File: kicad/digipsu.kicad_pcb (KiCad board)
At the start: 2 copper layers, 57 parts, among them J1 Screw_Terminal_01x03, J2 Screw_Terminal_01x03, Q1 BC337, Q2 BC327, Q3 2N6058, Q4 2N6058, Q5 IRLZ34N, U1 INA169, U2 MCP6002-xP, U3 Pico, U4 MCP6002-xP

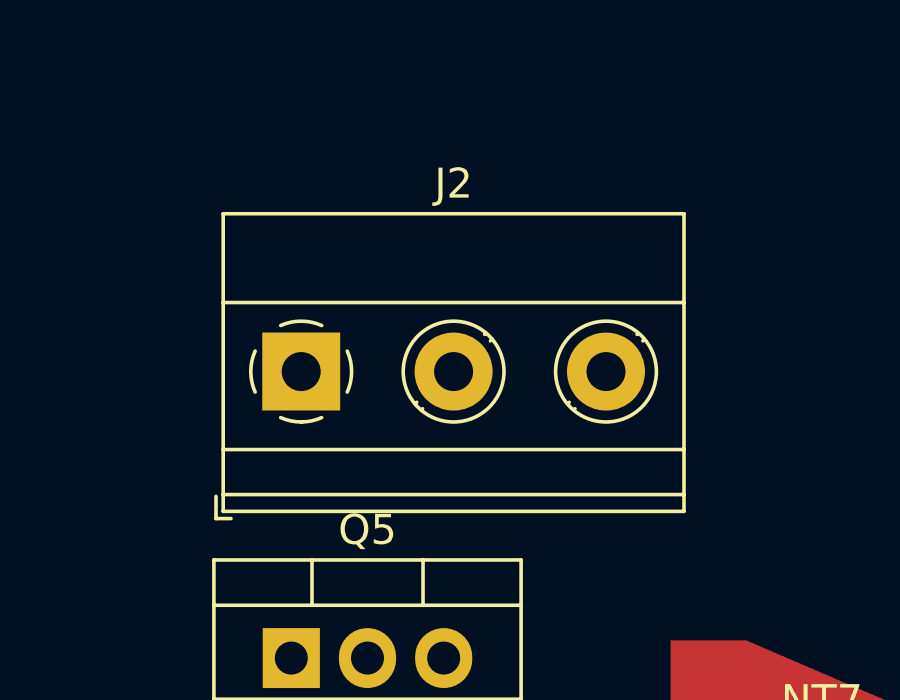
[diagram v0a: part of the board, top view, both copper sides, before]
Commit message: Small change for KiBot testing
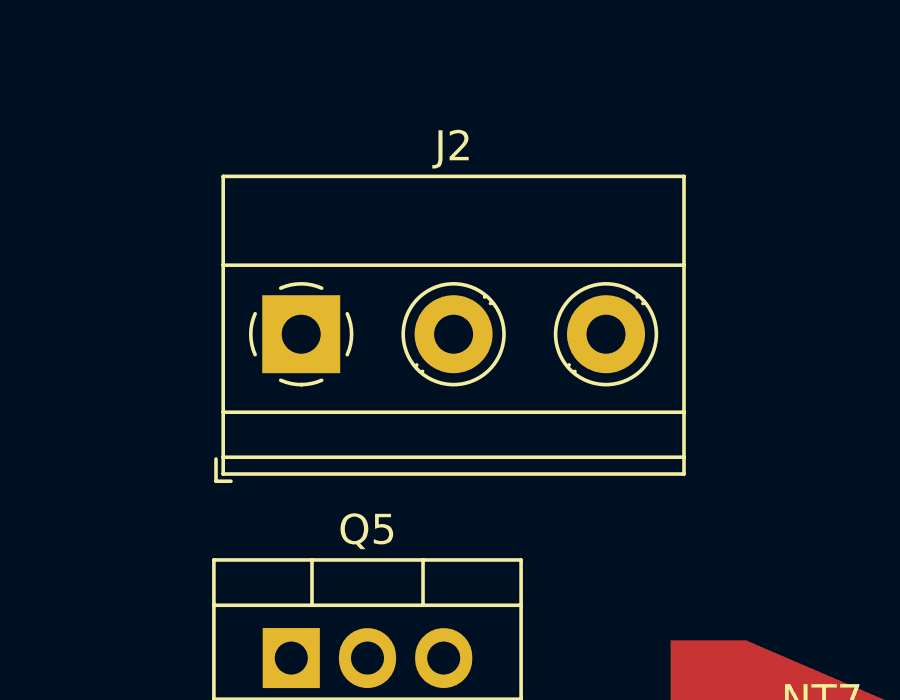
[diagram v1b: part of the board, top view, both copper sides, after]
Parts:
- moved J2 1.24 mm to (34.7, 27.9)
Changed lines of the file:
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@@
   )
   (footprint "TerminalBlock_Phoenix:TerminalBlock_Phoenix_MKDS-1,5-3-5.08_1x03_P5.08mm_Horizontal" (layer "F.Cu")
-    (at 34.715 29.185)
+    (at 34.715 27.94)
     (descr "Terminal Block Phoenix MKDS-1,5-3-5.08, 3 pins, pitch 5.08mm, size 15.2x9.8mm^2, drill diamater 1.3mm, pad diameter 2.6mm, see http://www.farnell.com/datasheets/100425.pdf, script-generated using https://github.com/pointhi/kicad-footprint-generator/scripts/TerminalBlock_Phoenix")
     (tags "THT Terminal Block Phoenix MKDS-1,5-3-5.08 pitch 5.08mm size 15.2x9.8mm^2 drill 1.3mm pad 2.6mm")

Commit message: Complete controller board
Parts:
- removed NT7: NetTie_2, Personal:NetTie_5mm_0.635mm
- added C1: C, Capacitor_THT:C_Disc_D3.8mm_W2.6mm_P2.50mm, F.Cu at (137.2, 83.8)
- added C10: C, Capacitor_THT:C_Disc_D3.8mm_W2.6mm_P2.50mm, F.Cu at (33.7, 144.1)
- added C11: C, Capacitor_THT:C_Disc_D3.8mm_W2.6mm_P2.50mm, F.Cu at (83.8, 189.2)
- added C12: 10µ, Capacitor_THT:C_Disc_D3.8mm_W2.6mm_P2.50mm, F.Cu at (67.9, 195.5)
- added C13: 100n, Capacitor_THT:C_Disc_D3.8mm_W2.6mm_P2.50mm, F.Cu at (64.8, 195.5)
- added C14: 100n, Capacitor_THT:C_Disc_D3.8mm_W2.6mm_P2.50mm, F.Cu at (38.1, 179.1)
- added C15: 100n, Capacitor_THT:C_Disc_D3.8mm_W2.6mm_P2.50mm, F.Cu at (21.6, 151.8)
- added C16: 10n, Capacitor_THT:C_Disc_D3.8mm_W2.6mm_P2.50mm, F.Cu at (102.2, 150.5)
- added C2: C, Capacitor_THT:C_Disc_D3.8mm_W2.6mm_P2.50mm, F.Cu at (137.2, 88.0)
- added C3: C, Capacitor_THT:C_Disc_D3.8mm_W2.6mm_P2.50mm, F.Cu at (137.2, 92.1)
- added C4: C, Capacitor_THT:C_Disc_D3.8mm_W2.6mm_P2.50mm, F.Cu at (96.5, 189.2)
- added C5: C, Capacitor_THT:C_Disc_D3.8mm_W2.6mm_P2.50mm, F.Cu at (91.4, 189.2)
- added C6: 10µ, Capacitor_THT:C_Disc_D3.8mm_W2.6mm_P2.50mm, F.Cu at (55.2, 195.5)
- added C7: 100n, Capacitor_THT:C_Disc_D3.8mm_W2.6mm_P2.50mm, F.Cu at (58.4, 195.5)
- added C8: 10µ, Capacitor_THT:C_Disc_D3.8mm_W2.6mm_P2.50mm, F.Cu at (73.0, 188.0)
- added C9: 100n, Capacitor_THT:C_Disc_D3.8mm_W2.6mm_P2.50mm, F.Cu at (69.8, 188.0)
- added H1: MountingHole, MountingHole:MountingHole_5mm, F.Cu at (24.1, 189.2)
- added H2: MountingHole, MountingHole:MountingHole_5mm, F.Cu at (110.5, 158.8)
- added H3: MountingHole, MountingHole:MountingHole_5mm, F.Cu at (50.8, 148.6)
- added J3: 8P8C, Connector_RJ:RJ45_Amphenol_54602-x08_Horizontal, F.Cu at (102.9, 191.8)
- added J4: 8P8C, Connector_RJ:RJ45_Amphenol_54602-x08_Horizontal, F.Cu at (27.9, 137.2)
- added J5: 8P8C, Connector_RJ:RJ45_Amphenol_54602-x08_Horizontal, F.Cu at (260.0, 96.3)
- added PS1: 1S4AE_1205S1.5UP, Converter_DCDC:Converter_DCDC_Murata_MEE1SxxxxSC_THT, F.Cu at (43.2, 147.3)
- added R39: 10k, Resistor_THT:R_Axial_DIN0207_L6.3mm_D2.5mm_P7.62mm_Horizontal, F.Cu at (78.1, 67.1)
- added R40: 1k, Resistor_THT:R_Axial_DIN0207_L6.3mm_D2.5mm_P7.62mm_Horizontal, F.Cu at (78.1, 71.1)
- added R41: 200, Potentiometer_THT:Potentiometer_Bourns_3296W_Vertical, F.Cu at (110.8, 89.3)
- added R42: 10, Resistor_THT:R_Axial_DIN0207_L6.3mm_D2.5mm_P7.62mm_Horizontal, F.Cu at (44.5, 188.0)
- added R43: 10, Resistor_THT:R_Axial_DIN0207_L6.3mm_D2.5mm_P7.62mm_Horizontal, F.Cu at (34.3, 188.0)
- added R44: 10, Resistor_THT:R_Axial_DIN0207_L6.3mm_D2.5mm_P7.62mm_Horizontal, F.Cu at (48.3, 184.2)
- added R45: 10, Resistor_THT:R_Axial_DIN0207_L6.3mm_D2.5mm_P7.62mm_Horizontal, F.Cu at (76.2, 195.6)
- added R46: 10, Resistor_THT:R_Axial_DIN0207_L6.3mm_D2.5mm_P7.62mm_Horizontal, F.Cu at (80.0, 195.6)
- added R47: 100, Resistor_THT:R_Axial_DIN0207_L6.3mm_D2.5mm_P7.62mm_Horizontal, F.Cu at (113.7, 176.5)
- added R48: 100, Resistor_THT:R_Axial_DIN0207_L6.3mm_D2.5mm_P7.62mm_Horizontal, F.Cu at (110.5, 176.5)
- added R49: 10k, Resistor_THT:R_Axial_DIN0207_L6.3mm_D2.5mm_P7.62mm_Horizontal, F.Cu at (29.2, 90.2)
- added R50: 10k, Resistor_THT:R_Axial_DIN0207_L6.3mm_D2.5mm_P7.62mm_Horizontal, F.Cu at (26.7, 93.3)
- added R51: 100, Resistor_THT:R_Axial_DIN0207_L6.3mm_D2.5mm_P7.62mm_Horizontal, F.Cu at (29.8, 167.6)
- added R52: 1k, Resistor_THT:R_Axial_DIN0207_L6.3mm_D2.5mm_P7.62mm_Horizontal, F.Cu at (29.8, 162.6)
- added R53: 100, Resistor_THT:R_Axial_DIN0207_L6.3mm_D2.5mm_P7.62mm_Horizontal, F.Cu at (19.1, 179.1)
- added R54: 1k, Resistor_THT:R_Axial_DIN0207_L6.3mm_D2.5mm_P7.62mm_Horizontal, F.Cu at (43.8, 175.3)
- added R55: 100, Resistor_THT:R_Axial_DIN0207_L6.3mm_D2.5mm_P7.62mm_Horizontal, F.Cu at (43.8, 154.9)
- added R56: 100, Resistor_THT:R_Axial_DIN0207_L6.3mm_D2.5mm_P7.62mm_Horizontal, F.Cu at (104.1, 176.5)
- added R57: 100, Resistor_THT:R_Axial_DIN0207_L6.3mm_D2.5mm_P7.62mm_Horizontal, F.Cu at (107.3, 176.5)
- added R58: 100, Resistor_THT:R_Axial_DIN0207_L6.3mm_D2.5mm_P7.62mm_Horizontal, F.Cu at (233.3, 105.3)
- added U10: Pico, MCU_RaspberryPi_and_Boards:RPi_Pico_SMD_TH, F.Cu at (219.7, 118.1)
- added U11: M24C32-RMN, Package_SO:SOIC-8_3.9x4.9mm_P1.27mm, F.Cu at (33.0, 85.7)
- added U12: SN75176BP, Package_DIP:DIP-8_W7.62mm, F.Cu at (26.7, 175.3)
- added U13: 6N137, Package_DIP:DIP-8_W7.62mm, F.Cu at (33.0, 167.6)
- added U14: SN75176BP, Package_DIP:DIP-8_W7.62mm, F.Cu at (233.4, 93.6)
- added U15: SN75176BP, Package_DIP:DIP-8_W7.62mm, F.Cu at (244.2, 93.6)
- added U5: L7805, Package_TO_SOT_THT:TO-220-3_Vertical, F.Cu at (86.4, 185.4)
- added U6: MCP3464R, Package_SO:TSSOP-20_4.4x6.5mm_P0.65mm, F.Cu at (62.2, 188.3)
- added U7: LF33_TO220, Package_TO_SOT_THT:TO-220-3_Vertical, F.Cu at (91.4, 193.0)
- added U8: 6N137, Package_DIP:DIP-8_W7.62mm, F.Cu at (40.6, 162.6)
- added U9: SN75176BP, Package_DIP:DIP-8_W7.62mm, F.Cu at (26.7, 162.6)
- J2: value Screw_Terminal_01x03 -> PWR IN
- NT6: footprint Personal:NetTie_5mm_0.635mm -> NetTie:NetTie-2_SMD_Pad0.5mm; moved to B.Cu
- Q1: value BC337 -> BC327
- Q2: value BC327 -> BC337
- R10, R11, R12, R13, R14, R15, R16, R17, R18, R19, R20, R21, R22, R23, R24, R25, R26, R27, R28, R29, R30, R31, R9: footprint Resistor_THT:R_Axial_DIN0207_L6.3mm_D2.5mm_P2.54mm_Vertical -> Resistor_THT:R_Axial_DIN0207_L6.3mm_D2.5mm_P7.62mm_Horizontal
- R32, R33: value 2K2 -> 10; footprint Resistor_THT:R_Axial_DIN0207_L6.3mm_D2.5mm_P2.54mm_Vertical -> Resistor_THT:R_Axial_DIN0207_L6.3mm_D2.5mm_P7.62mm_Horizontal
- R5: value 10k -> 100k
- R6: value 1k -> 10k
- R7: value 100k -> 1k
- moved R2 143.7 mm to (78.1, 46.8)
- moved R3 143.7 mm to (78.1, 50.9)
- moved U3 142.4 mm to (72.4, 167.6), turned to -90 degrees
- moved NT1 131.1 mm to (55.2, 191.1), turned to 90 degrees
- moved Q3 116.3 mm to (53.7, 53.8), turned to 0 degrees
- moved R35 114.0 mm to (78.1, 59.0), turned to 0 degrees
- moved R36 109.3 mm to (78.1, 63.0), turned to 0 degrees
- moved U2 105.4 mm to (88.9, 54.8), turned to 0 degrees
- moved NT6 100.7 mm to (73.0, 191.8), turned to 90 degrees
- moved J1 99.8 mm to (118.1, 87.9), turned to 0 degrees
- moved R38 99.0 mm to (110.8, 82.8)
- moved R37 84.4 mm to (110.8, 76.4), turned to 0 degrees
- moved J2 83.4 mm to (89.0, 91.2)
- moved U4 83.1 mm to (99.7, 54.8)
- moved R34 82.5 mm to (108.0, 29.2), turned to 0 degrees
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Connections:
- F1 pad 1: Net-(Q5-D) -> VBUS
- J1 pad 1: Net-(D1-A) -> Net-(J1-Pin_1)
- J1 pad 3: Net-(J1-Pin_3) -> GNDPWR
- J2 pad 1: Net-(D1-A) -> GNDPWR
- NT1 pad 1: Net-(F1-Pad2) -> /Controller/GND
- NT1 pad 2: VAA -> Net-(U6-DGND)
- NT3 pad 1: Net-(J1-Pin_3) -> Net-(J1-Pin_1)
- NT4 pad 1: Net-(J1-Pin_3) -> Net-(J1-Pin_1)
- NT5 pad 1: Net-(D1-A) -> GNDPWR
- NT6 pad 1: Net-(L1-Pad2) -> /Controller/GND
- NT6 pad 2: Net-(Q2-E) -> Net-(U6-AGND)
- Q1 pad 2: /Control voltage -> Net-(Q1-B)
- Q1 pad 3: Net-(Q1-E) -> VBUS
- Q2 pad 1: Net-(Q2-C) -> Net-(Q1-B)
- Q2 pad 2: Net-(Q1-C) -> unconnected-(Q2-B-Pad2)
- Q3 pad 1: Net-(Q2-C) -> Net-(Q1-C)
- Q4 pad 1: Net-(Q2-C) -> Net-(Q1-C)
- Q5 pad 1: /Buck PWM -> unconnected-(Q5-G-Pad1)
- Q5 pad 2: Net-(Q5-D) -> VBUS
- R1 pad 2: Net-(J1-Pin_3) -> Net-(J1-Pin_1)
- R10 pad 2: /DAC1 -> Net-(R10-Pad2)
- R11 pad 1: Net-(R10-Pad1) -> Net-(R11-Pad1)
- R11 pad 2: /DAC1 -> Net-(R10-Pad1)
- R12 pad 1: Net-(R10-Pad1) -> Net-(R12-Pad1)
- R12 pad 2: Net-(R12-Pad2) -> Net-(R11-Pad1)
- R13 pad 1: Net-(R12-Pad2) -> Net-(R13-Pad1)
- R13 pad 2: /DAC2 -> Net-(R12-Pad1)
- R14 pad 1: Net-(R12-Pad2) -> Net-(R14-Pad1)
- R14 pad 2: /DAC2 -> Net-(R13-Pad1)
- R15 pad 1: Net-(R12-Pad2) -> /Controller/Control Voltage
- R15 pad 2: Net-(R15-Pad2) -> Net-(R14-Pad1)
- R16 pad 1: Net-(R15-Pad2) -> Net-(R16-Pad1)
- R16 pad 2: /DAC3 -> /Controller/GND
- R17 pad 1: Net-(R15-Pad2) -> Net-(R10-Pad2)
- R17 pad 2: /DAC3 -> Net-(R16-Pad1)
- R18 pad 1: Net-(R15-Pad2) -> Net-(R10-Pad1)
- R18 pad 2: Net-(R18-Pad2) -> Net-(R10-Pad2)
- R19 pad 1: Net-(R18-Pad2) -> Net-(R11-Pad1)
- R19 pad 2: /DAC4 -> Net-(R10-Pad1)
- R20 pad 1: Net-(R18-Pad2) -> Net-(R12-Pad1)
- R20 pad 2: /DAC4 -> Net-(R11-Pad1)
- R21 pad 1: Net-(R18-Pad2) -> Net-(R13-Pad1)
- R21 pad 2: Net-(R21-Pad2) -> Net-(R12-Pad1)
- R22 pad 1: Net-(R21-Pad2) -> Net-(R14-Pad1)
- R22 pad 2: /DAC5 -> Net-(R13-Pad1)
- R23 pad 1: Net-(R21-Pad2) -> /Controller/Control Voltage
- R23 pad 2: /DAC5 -> Net-(R14-Pad1)
- R24 pad 1: Net-(R21-Pad2) -> Net-(R16-Pad1)
- R24 pad 2: Net-(R24-Pad2) -> /Controller/DAC1
- R25 pad 1: Net-(R24-Pad2) -> Net-(R10-Pad2)
- R25 pad 2: /DAC6 -> /Controller/DAC2
- R26 pad 1: Net-(R24-Pad2) -> Net-(R10-Pad1)
- R26 pad 2: /DAC6 -> /Controller/DAC3
- R27 pad 1: Net-(R24-Pad2) -> Net-(R11-Pad1)
- R27 pad 2: Net-(R27-Pad2) -> /Controller/DAC4
- R28 pad 1: Net-(R27-Pad2) -> Net-(R12-Pad1)
- R28 pad 2: /DAC7 -> /Controller/DAC5
- R29 pad 1: Net-(R27-Pad2) -> Net-(R13-Pad1)
- R29 pad 2: /DAC7 -> /Controller/DAC6
- R30 pad 1: Net-(R27-Pad2) -> Net-(R14-Pad1)
- R30 pad 2: Net-(R30-Pad2) -> /Controller/DAC7
- R31 pad 1: Net-(R30-Pad2) -> /Controller/Control Voltage
- R31 pad 2: /DAC8 -> /Controller/DAC8
- R32 pad 1: Net-(R30-Pad2) -> /Controller/SPI.SCK
- R32 pad 2: /DAC8 -> Net-(U6-SCK)
- R33 pad 1: Net-(R30-Pad2) -> /Controller/SPI.MISO
- R33 pad 2: /Control voltage -> Net-(U6-SDO)
- R4 pad 1: Net-(L1-Pad2) -> Net-(U4B-+)
- R5 pad 1: Net-(Q2-C) -> VBUS
- R5 pad 2: Net-(Q1-E) -> Net-(Q1-B)
- R6 pad 1: Net-(Q1-E) -> Net-(Q1-C)
- R6 pad 2: GND -> Net-(Q2-E)
- R7 pad 2: Net-(Q1-C) -> GNDD
- R8 pad 1: Net-(L1-Pad2) -> Net-(U4B-+)
- R9 pad 1: Net-(R10-Pad1) -> Net-(R10-Pad2)
- R9 pad 2: GND -> Net-(R16-Pad1)
- U2 pad 6: unconnected-(U2B---Pad6) -> Net-(U2B--)
- U3 pad 1: /DAC1 -> /Controller/DAC1
- U3 pad 10: /DAC8 -> /Controller/DAC8
- U3 pad 16: unconnected-(U3-GPIO12-Pad16) -> /Controller/TX
- U3 pad 17: unconnected-(U3-GPIO13-Pad17) -> /Controller/RX
- U3 pad 19: unconnected-(U3-GPIO14-Pad19) -> /Controller/PWM-out
- U3 pad 2: /DAC2 -> /Controller/DAC2
- U3 pad 21: unconnected-(U3-GPIO16-Pad21) -> /Controller/SPI.MISO
- U3 pad 22: unconnected-(U3-GPIO17-Pad22) -> /Controller/SPI.SS
- U3 pad 24: unconnected-(U3-GPIO18-Pad24) -> /Controller/SPI.SCK
- U3 pad 25: unconnected-(U3-GPIO19-Pad25) -> /Controller/SPI.MOSI
- U3 pad 26: unconnected-(U3-GPIO20-Pad26) -> /Controller/ADC_CLK
- U3 pad 31: unconnected-(U3-GPIO26_ADC0-Pad31) -> Net-(U3-GPIO26_ADC0)
- U3 pad 36: unconnected-(U3-3V3-Pad36) -> /Controller/+3.3VD
- U3 pad 38: unconnected-(U3-GND-Pad38) -> /Controller/GND
- U3 pad 39: unconnected-(U3-VSYS-Pad39) -> /Controller/+5V
- U3 pad 4: /DAC3 -> /Controller/DAC3
- U3 pad 5: /DAC4 -> /Controller/DAC4
- U3 pad 6: /DAC5 -> /Controller/DAC5
- U3 pad 7: /DAC6 -> /Controller/DAC6
- U3 pad 9: /DAC7 -> /Controller/DAC7
- U4 pad 5: unconnected-(U4B-+-Pad5) -> Net-(U4B-+)
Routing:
- net /Controller/GND: track 0.00 -> 261.8 mm
- net /Controller/12V: track 0.00 -> 120.5 mm, vias 0 -> 1
- net /Controller/Control Voltage: track 0.00 -> 106.3 mm
- net /Controller/PWM-out: track 0.00 -> 88.1 mm
- net Net-(Q2-C): track 87.9 -> 0.00 mm
- net /Controller/+5V: track 0.00 -> 87.9 mm
- net /Controller/CTRL.+5V: track 0.00 -> 78.2 mm, vias 0 -> 1
- net /Controller/CTRL.GND: track 0.00 -> 77.8 mm
- net /Controller/+3.3VD: track 0.00 -> 62.0 mm
- net /Controller/CTRL.RX-: track 0.00 -> 59.7 mm
- net Net-(U6-CH0): track 0.00 -> 59.7 mm
- net /Controller/CTRL.RX+: track 0.00 -> 59.5 mm
- net Net-(U6-CH2): track 0.00 -> 55.6 mm
- net Net-(U6-CH4): track 0.00 -> 51.9 mm
- net Net-(Q4-C): track 49.8 -> 0.00 mm
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- added copper zone on B.Cu, net (none)
- added copper zone on F.Cu, net (none)
- added copper zone on B.Cu, net GND
- added copper zone on F.Cu, net GND
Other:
- board outline added: 102.9 x 63.5 mm

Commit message: Add kibot config
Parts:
- added R59: 2K2, Resistor_THT:R_Axial_DIN0207_L6.3mm_D2.5mm_P7.62mm_Horizontal, F.Cu at (100.3, 130.6)
- added R60: 1K, Resistor_THT:R_Axial_DIN0207_L6.3mm_D2.5mm_P7.62mm_Horizontal, F.Cu at (100.3, 134.6)
- added SW1: RotaryEncoder_Switch, Rotary_Encoder:RotaryEncoder_Bourns_Vertical_PEC12R-3xxxF-Sxxxx, B.Cu at (71.3, 181.5)
- added SW2: RotaryEncoder_Switch, Rotary_Encoder:RotaryEncoder_Bourns_Vertical_PEC12R-3xxxF-Sxxxx, B.Cu at (42.9, 181.5)
- moved F1 285.3 mm to (372.6, 83.3)
- moved R2 285.3 mm to (361.3, 81.3)
- moved R3 285.3 mm to (361.3, 85.4)
- moved R34 285.3 mm to (391.1, 63.7)
- moved R4 285.3 mm to (319.6, 58.2)
- moved R8 285.3 mm to (319.6, 72.3)
- moved J1 234.8 mm to (347.3, 36.9)
- moved J2 234.8 mm to (318.1, 40.2)
- moved NT4 234.8 mm to (311.2, 37.1)
- moved NT5 234.8 mm to (311.2, 43.1)
- moved Q3 234.8 mm to (282.8, 2.81)
- moved Q5 234.8 mm to (319.7, 17.4)
- moved R35 234.8 mm to (307.2, 7.95)
- moved R36 234.8 mm to (307.2, 12.0)
- moved R37 234.8 mm to (340.0, 25.4)
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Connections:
- U10 pad 38: unconnected-(U10-GND-Pad38) -> /User Interface/CTRL.GND
- U10 pad 39: unconnected-(U10-VSYS-Pad39) -> /User Interface/CTRL.+5V
- U14 pad 2: unconnected-(U14-~{RE}-Pad2) -> /User Interface/CTRL.+5V
- U14 pad 3: unconnected-(U14-DE-Pad3) -> /User Interface/CTRL.+5V
- U14 pad 4: unconnected-(U14-D-Pad4) -> /User Interface/TX
- U14 pad 5: unconnected-(U14-GND-Pad5) -> /User Interface/CTRL.GND
- U14 pad 8: unconnected-(U14-VCC-Pad8) -> /User Interface/CTRL.+5V
- U15 pad 1: unconnected-(U15-R-Pad1) -> Net-(U15-R)
- U15 pad 2: unconnected-(U15-~{RE}-Pad2) -> /User Interface/CTRL.GND
- U15 pad 3: unconnected-(U15-DE-Pad3) -> /User Interface/CTRL.GND
- U15 pad 5: unconnected-(U15-GND-Pad5) -> /User Interface/CTRL.GND
- U15 pad 8: unconnected-(U15-VCC-Pad8) -> /User Interface/CTRL.+5V
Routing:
- net Net-(U11-SCL): track 13.9 -> 13.0 mm
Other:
- board size 102.9 x 63.5 mm -> 137.2 x 174.1 mm
- board text added: "Controller"
